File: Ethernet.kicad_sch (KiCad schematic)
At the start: 1 part, among them IC6 LAN8651B1-E_LMX

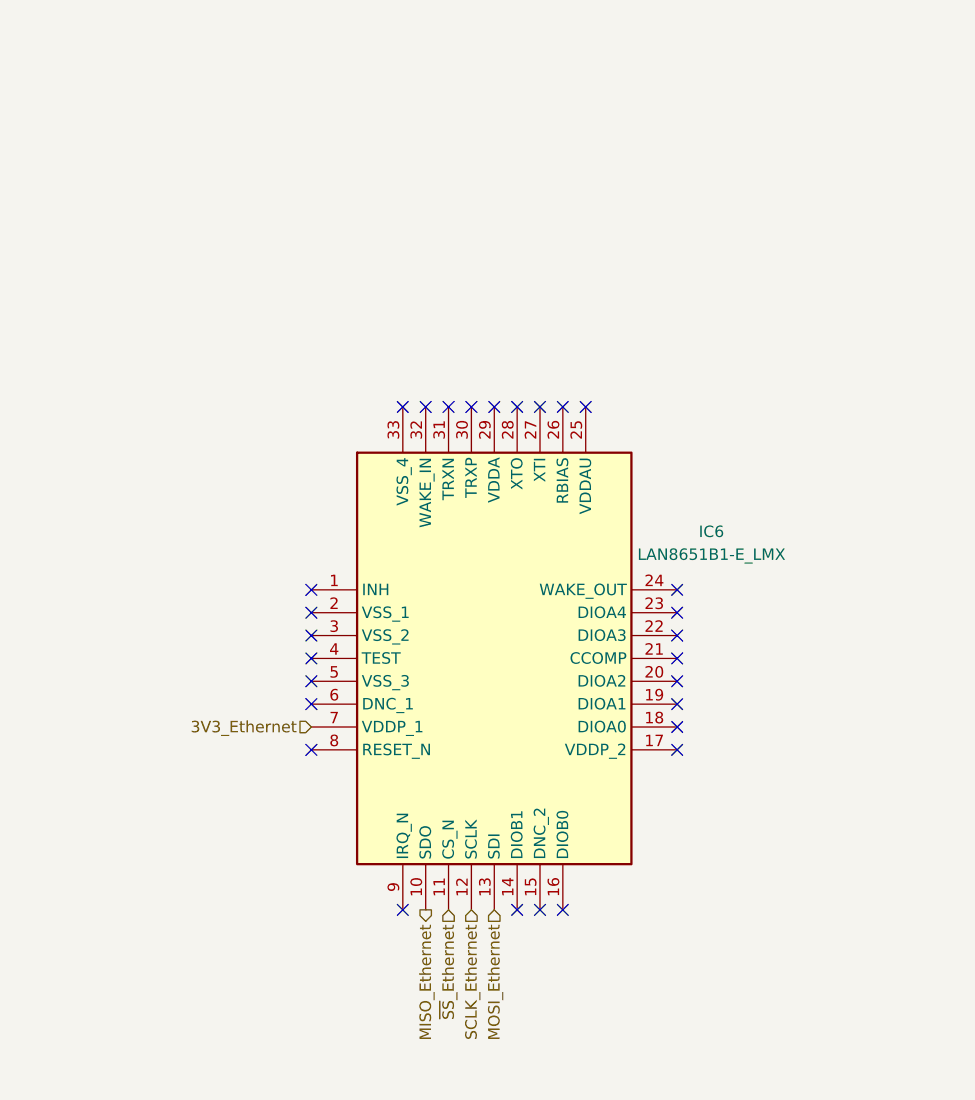
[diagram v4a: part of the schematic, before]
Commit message: Functionnal block delimiting in schematics
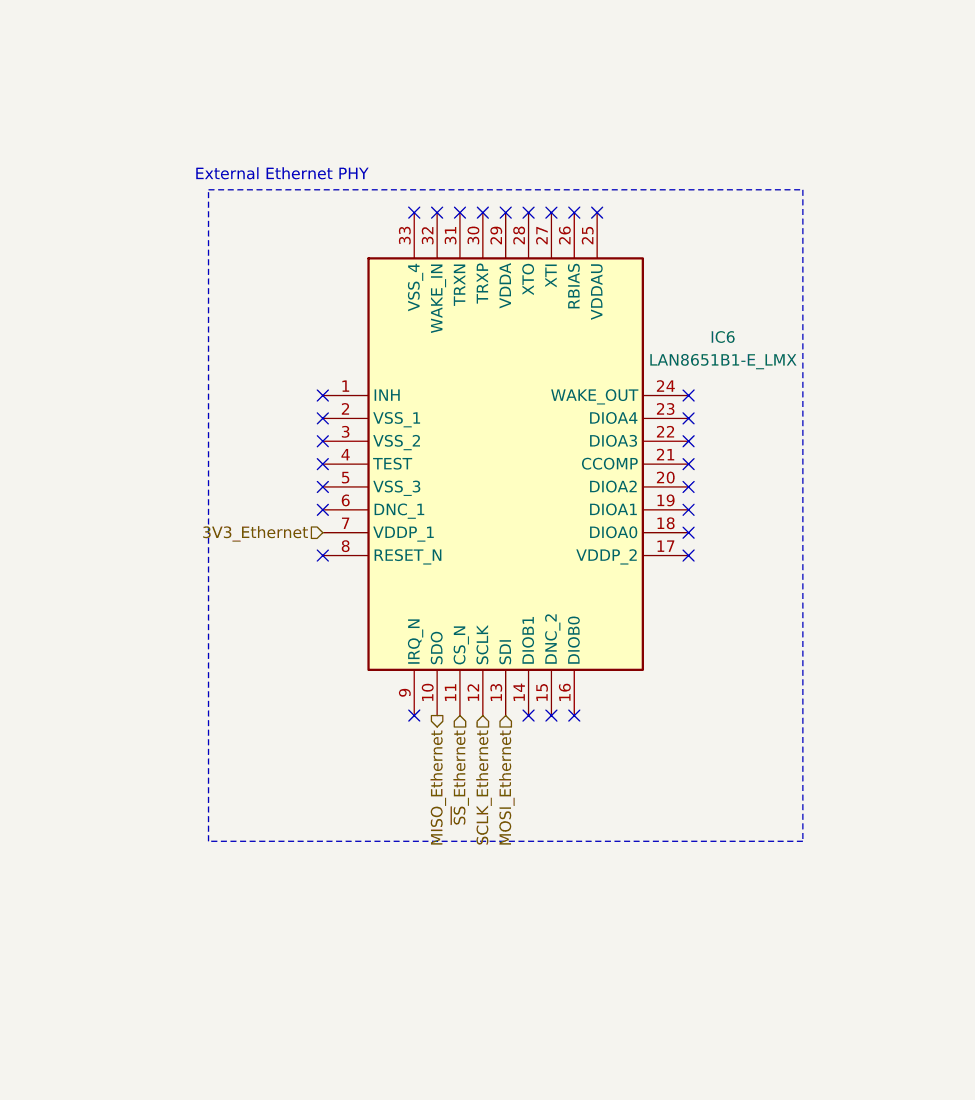
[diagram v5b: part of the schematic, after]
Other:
- note added: "External Ethernet PHY"
- moved on the sheet: IC6
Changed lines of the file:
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@@
 	(generator_version "9.0")
 	(paper "A4")
+	(rectangle
+		(start 111.76 67.31)
+		(end 177.8 139.7)
+		(stroke
+			(width 0)
+			(type dash)
+		)
+		(fill
+			(type none)
+		)
+	)
+	(text "External Ethernet PHY"
+		(exclude_from_sim no)
+		(at 119.888 65.786 0)
+		(effects
+			(font
+				(size 1.27 1.27)
+			)
+		)
+	)
 	(text "Ethernet PHY"
 		(exclude_from_sim no)
@@
 	)
 	(no_connect
-		(at 163.83 129.54)
-	)
-	(no_connect
-		(at 123.19 121.92)
-	)
-	(no_connect
-		(at 148.59 147.32)
-	)
-	(no_connect
-		(at 133.35 91.44)
-	)
-	(no_connect
-		(at 163.83 114.3)
-	)
-	(no_connect
-		(at 151.13 147.32)
-	)
-	(no_connect
-		(at 163.83 116.84)
-	)
-	(no_connect
-		(at 133.35 147.32)
-	)
-	(no_connect
-		(at 163.83 124.46)
-	)
-	(no_connect
-		(at 123.19 114.3)
-	)
-	(no_connect
-		(at 151.13 91.44)
-	)
-	(no_connect
-		(at 148.59 91.44)
-	)
-	(no_connect
-		(at 153.67 91.44)
-	)
-	(no_connect
-		(at 146.05 147.32)
-	)
-	(no_connect
-		(at 123.19 111.76)
-	)
-	(no_connect
-		(at 140.97 91.44)
-	)
-	(no_connect
-		(at 138.43 91.44)
-	)
-	(no_connect
-		(at 123.19 116.84)
-	)
-	(no_connect
-		(at 163.83 111.76)
-	)
-	(no_connect
-		(at 163.83 121.92)
-	)
-	(no_connect
-		(at 123.19 124.46)
-	)
-	(no_connect
-		(at 143.51 91.44)
-	)
-	(no_connect
-		(at 123.19 129.54)
-	)
-	(no_connect
-		(at 123.19 119.38)
-	)
-	(no_connect
-		(at 135.89 91.44)
-	)
-	(no_connect
-		(at 163.83 127)
-	)
-	(no_connect
-		(at 146.05 91.44)
-	)
-	(no_connect
-		(at 163.83 119.38)
+		(at 165.1 107.95)
+	)
+	(no_connect
+		(at 124.46 100.33)
+	)
+	(no_connect
+		(at 149.86 125.73)
+	)
+	(no_connect
+		(at 134.62 69.85)
+	)
+	(no_connect
+		(at 165.1 92.71)
+	)
+	(no_connect
+		(at 152.4 125.73)
+	)
+	(no_connect
+		(at 165.1 95.25)
+	)
+	(no_connect
+		(at 134.62 125.73)
+	)
+	(no_connect
+		(at 165.1 102.87)
+	)
+	(no_connect
+		(at 124.46 92.71)
+	)
+	(no_connect
+		(at 152.4 69.85)
+	)
+	(no_connect
+		(at 149.86 69.85)
+	)
+	(no_connect
+		(at 154.94 69.85)
+	)
+	(no_connect
+		(at 147.32 125.73)
+	)
+	(no_connect
+		(at 124.46 90.17)
+	)
+	(no_connect
+		(at 142.24 69.85)
+	)
+	(no_connect
+		(at 139.7 69.85)
+	)
+	(no_connect
+		(at 124.46 95.25)
+	)
+	(no_connect
+		(at 165.1 90.17)
+	)
+	(no_connect
+		(at 165.1 100.33)
+	)
+	(no_connect
+		(at 124.46 102.87)
+	)
+	(no_connect
+		(at 144.78 69.85)
+	)
+	(no_connect
+		(at 124.46 107.95)
+	)
+	(no_connect
+		(at 124.46 97.79)
+	)
+	(no_connect
+		(at 137.16 69.85)
+	)
+	(no_connect
+		(at 165.1 105.41)
+	)
+	(no_connect
+		(at 147.32 69.85)
+	)
+	(no_connect
+		(at 165.1 97.79)
 	)
 	(hierarchical_label "MOSI_Ethernet"
 		(shape input)
-		(at 143.51 147.32 270)
+		(at 144.78 125.73 270)
 		(effects
 			(font
@@
 	(hierarchical_label "~{SS}_Ethernet"
 		(shape input)
-		(at 138.43 147.32 270)
+		(at 139.7 125.73 270)
 		(effects
 			(font
@@
 	(hierarchical_label "MISO_Ethernet"
 		(shape output)
-		(at 135.89 147.32 270)
+		(at 137.16 125.73 270)
 		(effects
 			(font
@@
 	(hierarchical_label "SCLK_Ethernet"
 		(shape input)
-		(at 140.97 147.32 270)
+		(at 142.24 125.73 270)
 		(effects
 			(font
@@
 	(hierarchical_label "3V3_Ethernet"
 		(shape input)
-		(at 123.19 127 180)
+		(at 124.46 105.41 180)
 		(effects
 			(font
@@
 	(symbol
 		(lib_id "weather-station-poc-sym:LAN8651B1-E_LMX")
-		(at 123.19 111.76 0)
+		(at 124.46 90.17 0)
 		(unit 1)
 		(exclude_from_sim no)
@@
 		(fields_autoplaced yes)
 		(property "Reference" "IC6"
-			(at 167.64 105.3045 0)
+			(at 168.91 83.7145 0)
 			(effects
 				(font
@@
 		)
 		(property "Value" "LAN8651B1-E_LMX"
-			(at 167.64 107.8445 0)
+			(at 168.91 86.2545 0)
 			(effects
 				(font
@@
 		)
 		(property "Footprint" "weather-station-poc-fp:QFN50P500X500X100-33N-D"
-			(at 160.02 193.98 0)
+			(at 161.29 172.39 0)
 			(effects
 				(font
@@
 		)
 		(property "Datasheet" "https://ww1.microchip.com/downloads/aemDocuments/documents/AIS/ProductDocuments/DataSheets/LAN8650-1-Data-Sheet-60001734.pdf"
-			(at 160.02 293.98 0)
+			(at 161.29 272.39 0)
 			(effects
 				(font
@@
 		)
 		(property "Description" "Ethernet ICs 10BASE-T1S MAC-PHY with SPI"
-			(at 123.19 111.76 0)
+			(at 124.46 90.17 0)
 			(effects
 				(font
@@
 		)
 		(property "Height" "1"
-			(at 160.02 493.98 0)
+			(at 161.29 472.39 0)
 			(effects
 				(font
@@
 		)
 		(property "Mouser Part Number" "579-LAN8651B1-E/LMX"
-			(at 160.02 593.98 0)
+			(at 161.29 572.39 0)
 			(effects
 				(font
@@
 		)
 		(property "Mouser Price/Stock" "https://www.mouser.co.uk/ProductDetail/Microchip-Technology/LAN8651B1-E-LMX?qs=HoCaDK9Nz5cTGz8XEJbodA%3D%3D"
-			(at 160.02 693.98 0)
+			(at 161.29 672.39 0)
 			(effects
 				(font
@@
 		)
 		(property "Manufacturer_Name" "Microchip"
-			(at 160.02 793.98 0)
+			(at 161.29 772.39 0)
 			(effects
 				(font
@@
 		)
 		(property "Manufacturer_Part_Number" "LAN8651B1-E/LMX"
-			(at 160.02 893.98 0)
-			(effects
-				(font
+			(at 161.29 872.39 0)
+			(effects
+				(font

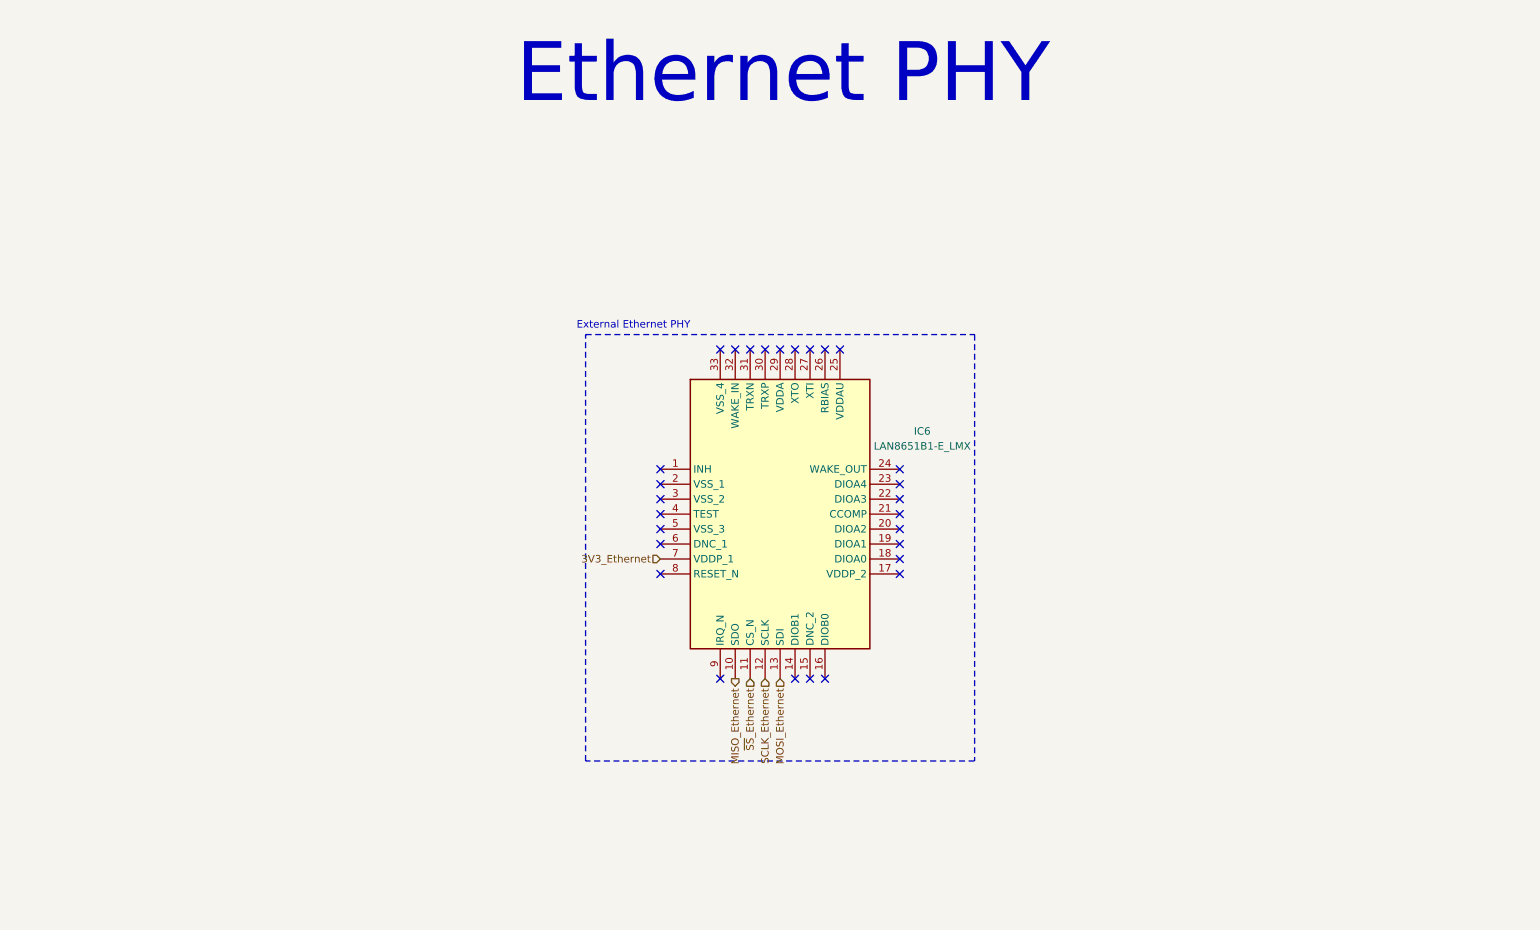
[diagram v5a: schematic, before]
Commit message: Prepare Ethernet schematic (LAN8651)
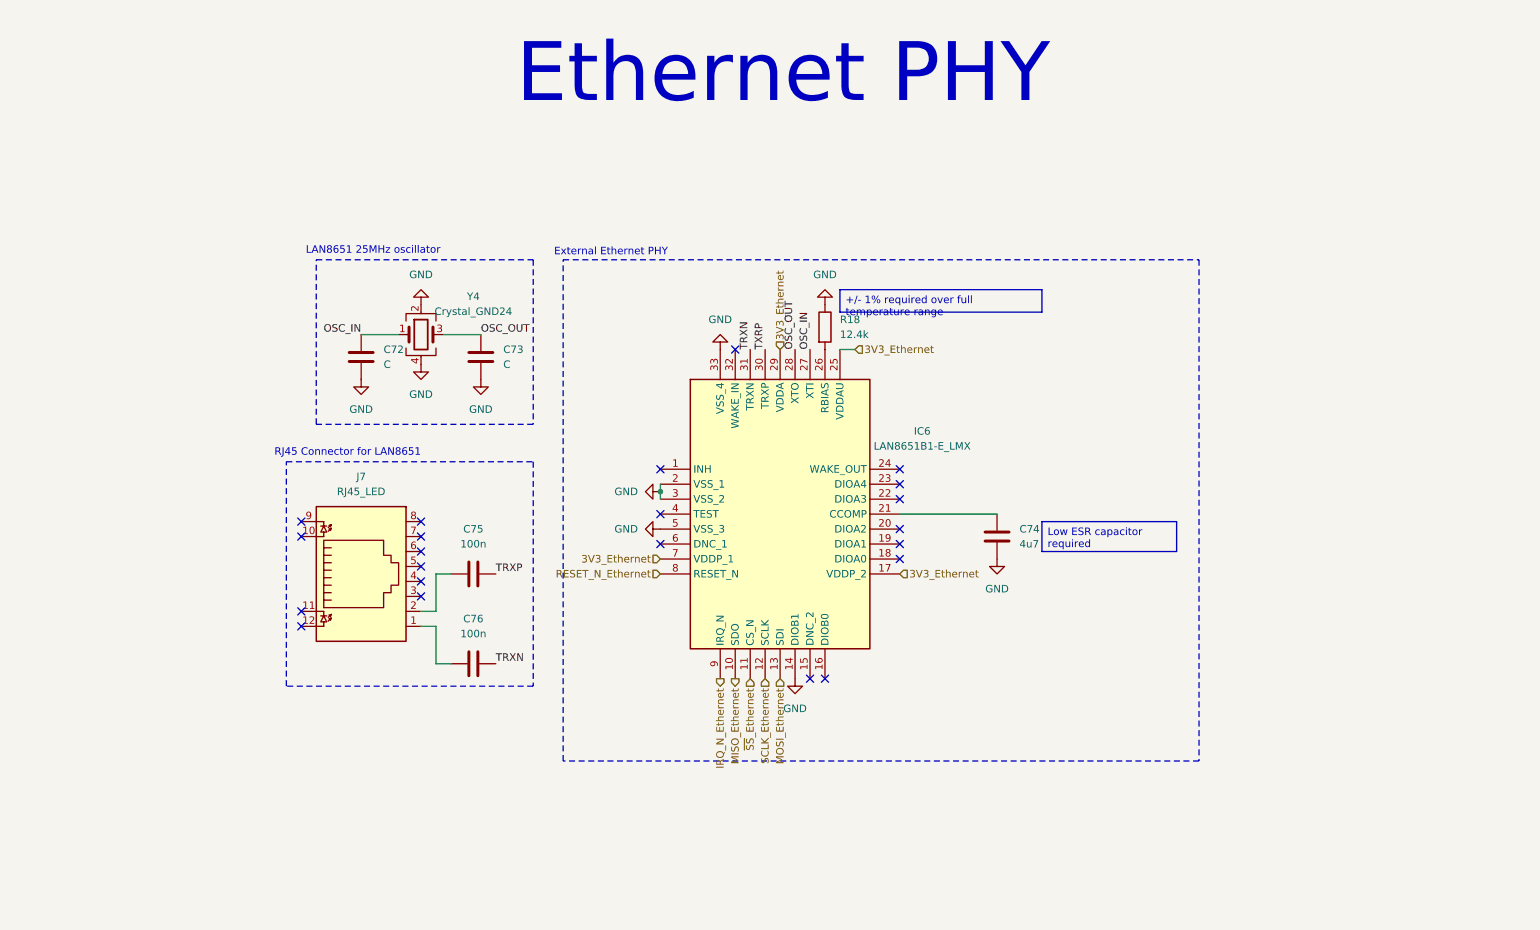
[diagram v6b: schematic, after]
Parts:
- added C72, C73: C, symbol Device:C
- added C74: 4u7, symbol Device:C
- added C75, C76: 100n, symbol Device:C
- added J7: RJ45_LED, Connector_RJ:RJ45_Amphenol_54602-x08_Horizontal, symbol Connector:RJ45_LED
- added R18: 12.4k, symbol Device:R
- added Y4: Crystal_GND24, symbol Device:Crystal_GND24
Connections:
- net 3V3_Ethernet: now also IC6.17 (VDDP_2), IC6.25 (VDDAU), IC6.29 (VDDA)
- net GND: now reaches IC6.14 (DIOB1)
- net GND: now also IC6.2 (VSS_1), IC6.3 (VSS_2), IC6.33 (VSS_4), IC6.5 (VSS_3), C72.2, C73.2, C74.2, R18.1, Y4.2, Y4.4
- net at IC6.21 (CCOMP): now also C74.1
- net at IC6.26 (RBIAS): now also R18.2
- net OSC_IN: now reaches IC6.27 (XTI)
- net OSC_IN: now also C72.1, Y4.1
- net OSC_OUT: now reaches IC6.28 (XTO)
- net OSC_OUT: now also C73.1, Y4.3
- net TXRP: now reaches IC6.30 (TRXP)
- net TRXN: now reaches IC6.31 (TRXN)
- net TRXN: now also C76.2
- net RESET_N_Ethernet: now reaches IC6.8 (RESET_N)
- net IRQ_N_Ethernet: now reaches IC6.9 (IRQ_N)
- new net: C75.1, J7.2
- new net: C76.1, J7.1
- new net TRXP: C75.2
- no-connect marks 28 -> 22
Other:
- note added: "LAN8651 25MHz oscillator"
- note added: "RJ45 Connector for LAN8651"

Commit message: Update Ethernet.kicad_sch
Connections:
- net TXRP is gone; now on net TRXP: IC6.30 (TRXP)
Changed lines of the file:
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@@
 		)
 	)
-	(label "TXRP"
+	(label "TRXP"
 		(at 142.24 69.85 90)
 		(effects
